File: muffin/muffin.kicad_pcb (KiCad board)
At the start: 2 copper layers, 76.2 x 94.5 mm, 45 parts, among them J1 USB_C_Receptacle_USB2.0, J2 AVR-ISP-6, SW1 RotaryEncoder_Switch, SW2 SW1.A, SW3 SW1.B, SW4 SW2.B, SW5 SW1.C, SW6 SW2.C, SW7 SW_Push, SW8 SW_DIP_x01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

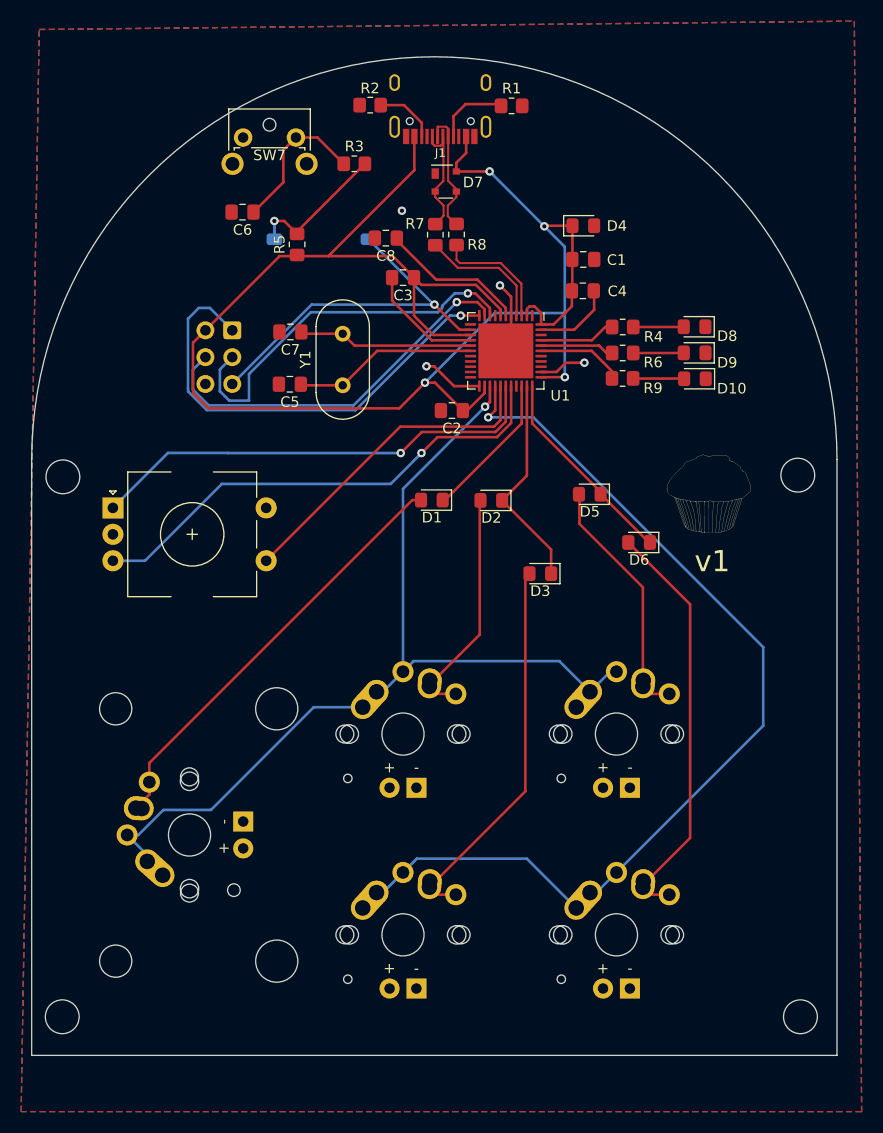
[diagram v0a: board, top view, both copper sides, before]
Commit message: Update switches footprint
I was using the LED version of the footprint for all 1U switches.
I didn't change the 2U footprint as that would have required
updating the Keebio library.
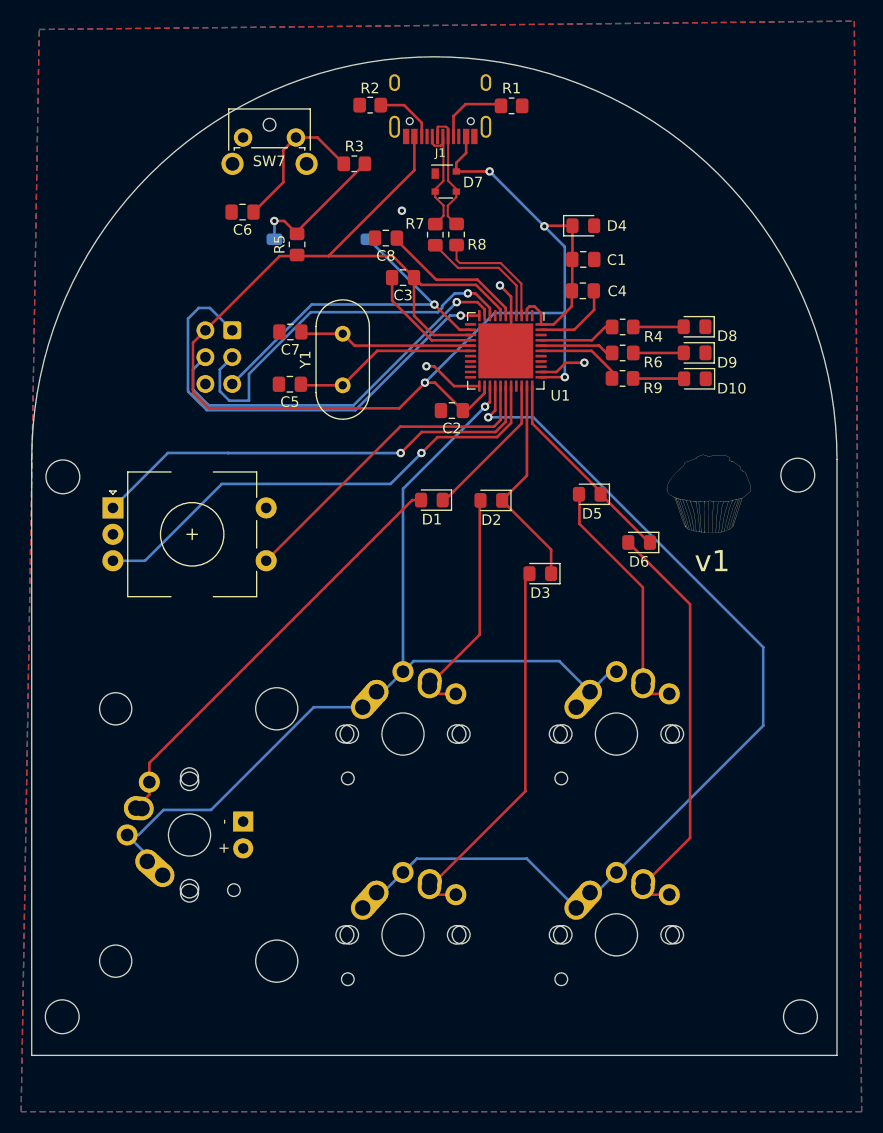
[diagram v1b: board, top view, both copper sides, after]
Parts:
- SW3, SW4, SW5, SW6: footprint Keebio:MX-Alps-Choc-1U -> Keebio:MX-Alps-Choc-1U-NoLED
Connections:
- SW3 pad 1: Row 1 -> Net-(D2-Pad2)
- SW3 pad 2: Net-(D2-Pad2) -> Row 1
- SW4 pad 1: Row 2 -> Net-(D3-Pad2)
- SW4 pad 2: Net-(D3-Pad2) -> Row 2
- SW5 pad 1: Row 1 -> Net-(D5-Pad2)
- SW5 pad 2: Net-(D5-Pad2) -> Row 1
- SW6 pad 1: Row 2 -> Net-(D6-Pad2)
- SW6 pad 2: Net-(D6-Pad2) -> Row 2
